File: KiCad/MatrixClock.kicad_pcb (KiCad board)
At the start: 2 copper layers, 160 x 32 mm, 69 parts, among them J1 USB_OTG, J2 CONN_01X06, J3 CONN_01X05, J4 CONN_01X05, J5 DISP_PWR, M1 Module_MAX7219, M2 Module_MAX7219, M3 Module_MAX7219, M4 Module_MAX7219, M5 Module_MAX7219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

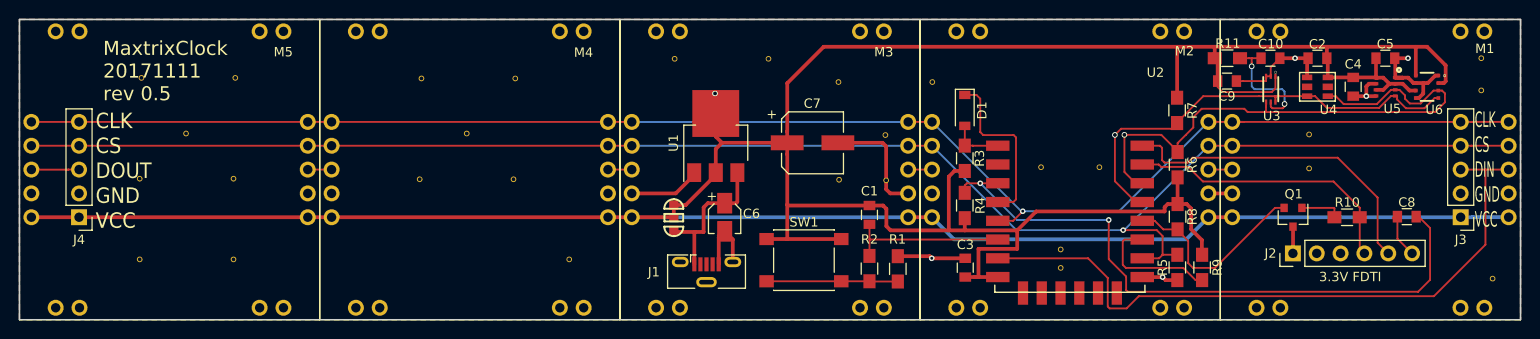
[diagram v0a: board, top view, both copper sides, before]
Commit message: New release 0.6, discovered a stray stitch via in the middle of the regulator solder pad. Moved other stitch via's around for a more visual appealing pattern ^^
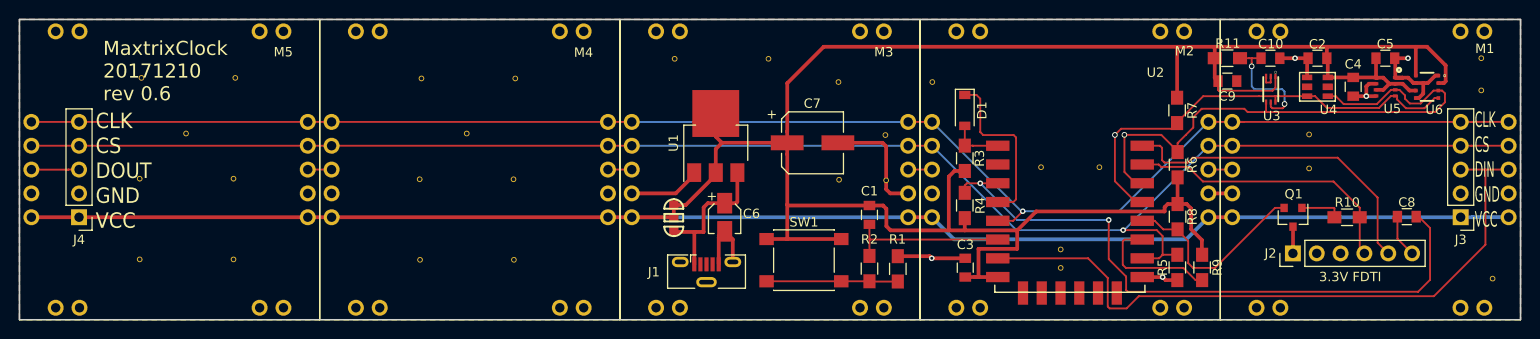
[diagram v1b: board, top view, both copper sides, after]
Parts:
- added VIA23: VIA-6mm, Private:VIA-6mm, F.Cu at (69.7, 45.6)
- moved VIA23 5.89 mm to (79.7, 45.6)
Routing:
- net GND: track 72.9 -> 68.2 mm
- net +3V3: vias 1 -> 0
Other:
- board text added: "MaxtrixClock 20171210 rev 0.6"
- board text removed: "MaxtrixClock 20171111 rev 0.5"
